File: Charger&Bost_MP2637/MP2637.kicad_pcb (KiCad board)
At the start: 2 copper layers, 43 x 17.5 mm, 46 parts

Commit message: MP2637: засстановка компонентов...
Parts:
- removed C11: 47uF, Capacitors:CAP1206
- C8: footprint Capacitors:CAP0805 -> Capacitors:CAP0603
- C9: footprint Capacitors:CAP0603 -> Capacitors:CAP0805
- GB1: footprint Connectors:for_PolarOut_PLL1.27-2 -> Connectors:for_PolarOut_PLS-2
- XP3: footprint Connectors:PLS2-2 -> Connectors:PLS-2
- moved R11 51.1 mm to (117.8, 55.5), turned to 180 degrees
- moved R12 49.7 mm to (117.8, 59.5), turned to 180 degrees
- moved R13 46.1 mm to (117.8, 65.0), turned to 180 degrees
- moved R2 45.6 mm to (123.5, 60.2)
- moved R8 45.2 mm to (123.5, 56.8), turned to 180 degrees
- moved R7 45.0 mm to (123.5, 53.2), turned to 180 degrees
- moved GB1 44.0 mm to (144.0, 53.6), turned to 270 degrees
- moved R16 43.9 mm to (132.0, 53.2)
- moved C6 42.2 mm to (126.0, 52.5), turned to 90 degrees
- moved R6 42.0 mm to (123.5, 55.0)
- moved R17 41.8 mm to (132.2, 51.2)
- moved HL1 41.4 mm to (118.0, 53.5)
- moved C2 40.9 mm to (113.8, 58.8), turned to 90 degrees
- moved R5 40.4 mm to (129.5, 52.5), turned to 90 degrees
- moved R4 39.3 mm to (127.8, 52.5), turned to 270 degrees
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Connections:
- C10 pad 1: /+BATT -> +5V
- C8 pad 1: +5V -> /+BATT
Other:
- net class Default: trace_width 0.3 -> 0.2
- net class wide: trace_width 0.7 -> 0.5
- net class wide wide: trace_width 1.2 -> 1

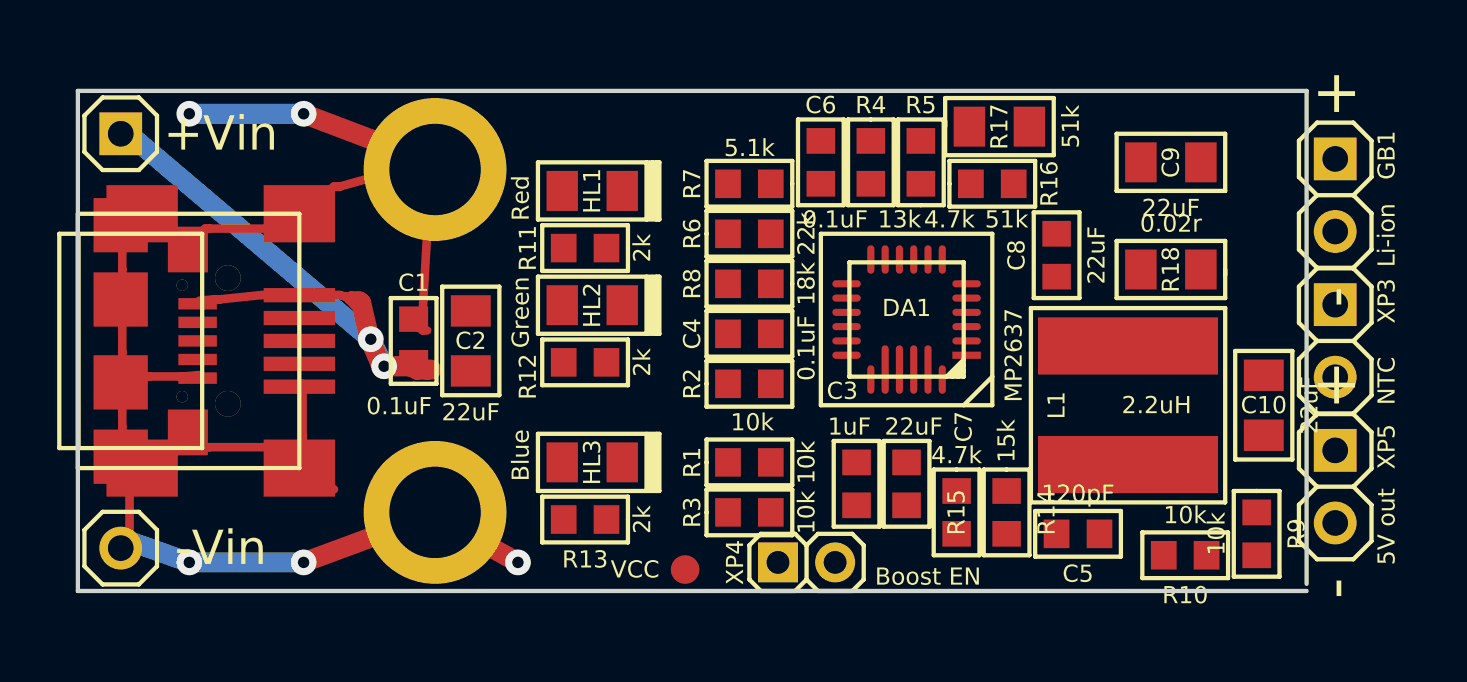
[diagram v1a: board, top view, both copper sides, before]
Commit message: MP2637: расстановка компонентов завершена
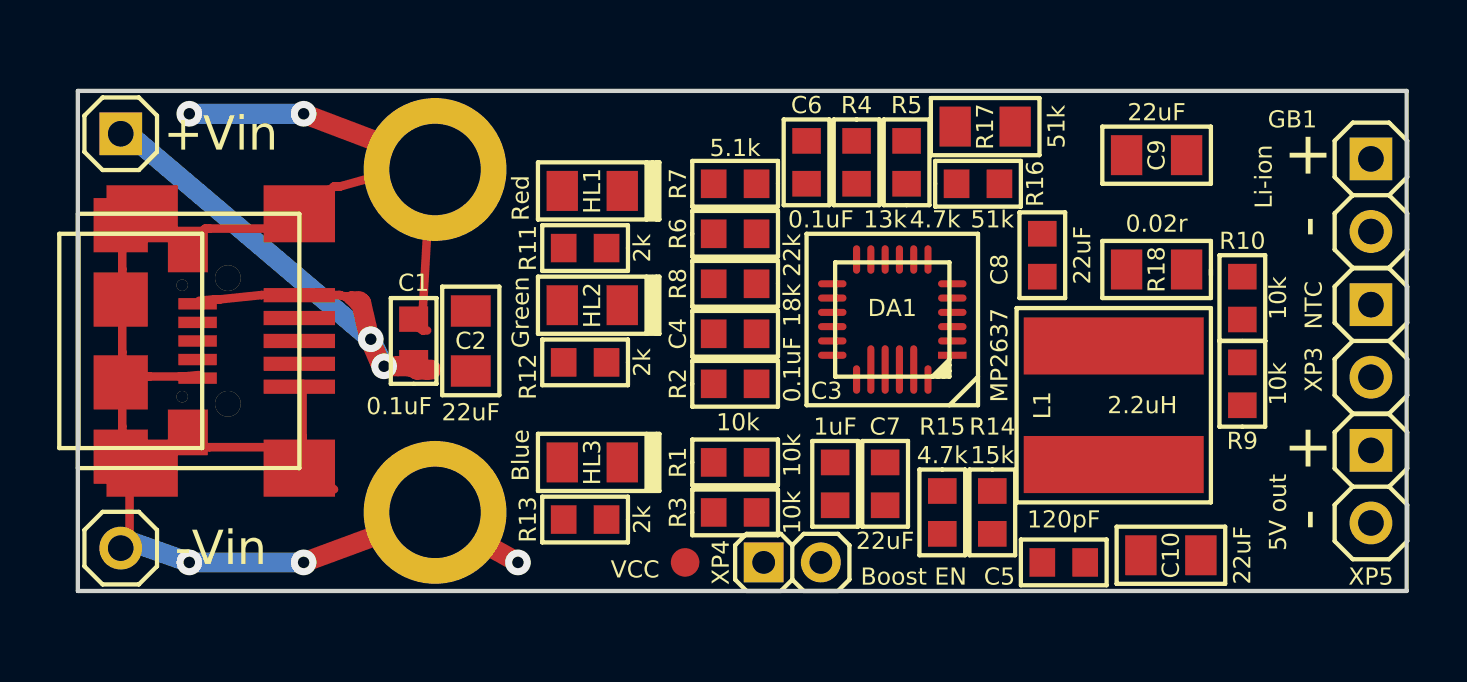
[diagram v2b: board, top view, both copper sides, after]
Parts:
- moved R10 9.22 mm to (140.8, 57.2), turned to 90 degrees
- moved C10 6.17 mm to (138.2, 66.2), turned to 0 degrees
- moved R9 5.27 mm to (140.8, 60.2), turned to 90 degrees
- moved Label1 3.21 mm to (133.2, 78.2)
- moved GB1 1.25 mm to (145.2, 53.6)
- moved XP3 1.25 mm to (145.2, 58.8)
- moved XP5 1.25 mm to (145.2, 63.9)
- moved C5 1.12 mm to (134.5, 66.5)
- moved C3 0.75 mm to (126.5, 63.8)
- moved C7 0.75 mm to (128.2, 63.8)
- moved C9 0.56 mm to (137.8, 52.2), turned to 180 degrees
- moved C4 0.50 mm to (123.0, 58.5)
- moved C6 0.50 mm to (125.5, 52.5)
- moved C8 0.50 mm to (133.8, 55.8)
- moved DA1 0.50 mm to (128.5, 58.0)
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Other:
- board size 43 x 17.5 mm -> 46.5 x 17.5 mm
- board text added: "C3 : Cin C6 : Ctmr C7 : Csys C8 : Cbatt R4 : R3 R5 : R5 R6 : R4 (RH) R7 : R6 (RL) R8 : Rilim R9 : RT1 R10 : RT2 R14 : R1 R15 : R2 R16 : Rolim R17 : Riset R18 : RS1"
- board text added: "Green : Charging Red : AC ok Blue : Boost EN"

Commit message: MP2637: Трассировка завершена
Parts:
- added J1: Jumper, Power:Jump_0.5mm, B.Cu at (130.8, 57.5)
- Hole1, Hole2: moved to B.Cu
- moved Label1 7.85 mm to (125.4, 78.4)
- moved R14 0.50 mm to (132.0, 65.2)
- moved R15 0.50 mm to (130.2, 65.2)
- moved R2 0.24 mm to (123.0, 60.5)
- moved R10 0.06 mm to (140.8, 57.2)
- turned Hole1 to 180 degrees
- turned Hole2 to 180 degrees
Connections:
- C1 pad 2: GND -> GNDP
- C10 pad 2: GND -> GNDP
- C2 pad 2: GND -> GNDP
- C3 pad 2: GND -> GNDP
- C7 pad 2: GND -> GNDP
- C8 pad 2: GND -> GNDP
- C9 pad 2: GND -> GNDP
- DA1 pad 1: GND -> GNDP
- DA1 pad 23: GND -> GNDP
- DA1 pad 24: GND -> GNDP
- GB1 pad 2: GND -> GNDP
- Hole1 pad H: GND -> GNDP
- Hole2 pad H: GND -> GNDP
- XP2 pad 1: GND -> GNDP
- XP5 pad 2: GND -> GNDP
- XS1 pad 5: GND -> GNDP
- XS1 pad SHLD: GND -> GNDP
- XS2 pad 5: GND -> GNDP
- XS2 pad SHLD: GND -> GNDP
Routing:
- net GNDP: track 0.00 -> 202.3 mm, vias 0 -> 25
- net +5V: track 0.00 -> 49.5 mm, vias 0 -> 3
- net +USBvcc: track 22.9 -> 63.0 mm
- net /~BOST: track 0.00 -> 23.5 mm, vias 0 -> 2
- net /FB: track 0.00 -> 20.8 mm, vias 0 -> 2
- net /NTC: track 0.00 -> 20.8 mm, vias 0 -> 2
- net /+BATT: track 0.00 -> 17.5 mm
- net /VCC: track 0.00 -> 14.4 mm, vias 0 -> 2
- net /~CHG: track 0.00 -> 14.2 mm, vias 0 -> 2
- net GND: track 64.1 -> 76.3 mm, vias 5 -> 9
- net /LX2: track 0.00 -> 10.6 mm
- net /~ACOK: track 0.00 -> 10.0 mm, vias 0 -> 2
- net /LX1: track 0.00 -> 9.07 mm
- net /MODE: track 0.00 -> 8.38 mm, vias 0 -> 2
- net /~EN: track 0.00 -> 6.13 mm, vias 0 -> 2
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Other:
- net class Default: via_dia 0.9 -> 0.7; via_drill 0.4 -> 0.3
- net class wide: via_dia 0.9 -> 0.7; via_drill 0.4 -> 0.3
- net class wide 5V added: clearance 0.2, trace_width 0.7, via_dia 0.7, via_drill 0.3
- net class wide wide: via_dia 0.9 -> 0.7; via_drill 0.4 -> 0.3

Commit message: MP2637: проектировка завершена
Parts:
- moved Label1 20.6 mm to (132.2, 59.0)
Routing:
- net GNDP: track 202.3 -> 311.3 mm, vias 25 -> 48
- net GND: track 76.3 -> 77.6 mm
- added copper zone on B.Cu, net GNDP
- added copper zone on F.Cu, net GNDP
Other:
- board text added: "+Vin"
- board text added: "-Vin"
- board text added: "5V out"
- board text added: "Blue -> Boost EN"
- board text added: "Boost EN"
- board text added: "Green -> Charging"
- board text added: "Li-ion"
- board text added: "NTC"
- board text added: "Red -> AC ok"
- board text removed: "C3 : Cin C6 : Ctmr C7 : Csys C8 : Cbatt R4 : R3 R5 : R5 R6 : R4 (RH) R7 : R6 (RL) R8 : Rilim R9 : RT1 R10 : RT2 R14 : R1 R15 : R2 R16 : Rolim R17 : Riset R18 : RS1"
- board text removed: "Green : Charging Red : AC ok Blue : Boost EN"
